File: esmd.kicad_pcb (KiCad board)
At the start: 2 copper layers, 30 x 25 mm, 8 parts, among them J1 Conn_01x04, J2 Conn_01x08, J3 Conn_01x02, J4 Conn_01x02, U2 LM78M05_TO252, U3 74HC245

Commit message: Make it triple.
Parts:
- added C2: 100n, Capacitor_SMD:C_0603_1608Metric, F.Cu at (168.0, 120.0)
- added C3: 100n, Capacitor_SMD:C_0603_1608Metric, F.Cu at (167.9, 134.6)
- added H1: MountingHole, MountingHole:MountingHole_3.2mm_M3, F.Cu at (167.3, 86.1)
- added H2: MountingHole, MountingHole:MountingHole_3.2mm_M3, F.Cu at (167.3, 139.2)
- added J5: Conn_01x04, Connector_JST:JST_XH_B4B-XH-A_1x04_P2.50mm_Vertical, F.Cu at (159.5, 127.2)
- added J6: Conn_01x08, Connector_JST:JST_XH_B6B-XH-A_1x06_P2.50mm_Vertical, F.Cu at (177.4, 139.6)
- added J7: Conn_01x02, Connector_JST:JST_XH_B2B-XH-A_1x02_P2.50mm_Vertical, F.Cu at (158.5, 88.2)
- added R2: 1k, Resistor_SMD:R_0603_1608Metric, F.Cu at (164.6, 120.0)
- added R3: 1k, Resistor_SMD:R_0603_1608Metric, F.Cu at (164.6, 134.6)
- added U1: 74HC245, Package_SO:SSOP-20_5.3x7.2mm_P0.65mm, F.Cu at (167.8, 115.1)
- added U4: 74HC245, Package_SO:SSOP-20_5.3x7.2mm_P0.65mm, F.Cu at (167.8, 129.8)
- J1: footprint Connector_JST:JST_XH_S4B-XH-A_1x04_P2.50mm_Horizontal -> Connector_JST:JST_XH_B4B-XH-A_1x04_P2.50mm_Vertical
- J2: footprint Connector_JST:JST_XH_S6B-XH-A_1x06_P2.50mm_Horizontal -> Connector_JST:JST_XH_B6B-XH-A_1x06_P2.50mm_Vertical
- J3: value Conn_01x02 -> Conn_01x04; footprint Connector_JST:JST_XH_B2B-XH-A_1x02_P2.50mm_Vertical -> Connector_JST:JST_XH_B4B-XH-A_1x04_P2.50mm_Vertical
- J4: value Conn_01x02 -> Conn_01x08; footprint Connector_PinSocket_2.54mm:PinSocket_1x02_P2.54mm_Vertical -> Connector_JST:JST_XH_B6B-XH-A_1x06_P2.50mm_Vertical
- moved J4 37.9 mm to (177.4, 121.0), turned to 90 degrees
- moved J3 26.2 mm to (159.5, 111.7)
- moved C1 3.18 mm to (167.9, 106.2)
- moved R1 3.17 mm to (164.5, 106.2)
- moved U2 3.09 mm to (168.9, 93.2)
- moved U3 3.05 mm to (167.6, 101.1)
- moved J2 0.89 mm to (177.4, 102.3)
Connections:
- net Dir renamed Dir1
- net Dir_out renamed Dir_out1
- net Enable renamed Enable1
- net Enable_out renamed Enable_out1
- net Step renamed Step1
- net Step_out renamed Step_out1
- J3 pad 1: Net-(J3-Pin_1) -> Enable2
- J3 pad 2: GND -> Step2
- J4 pad 1: Net-(J3-Pin_1) -> Dir_out2
- U2 pad 1: Net-(J3-Pin_1) -> Net-(J7-Pin_1)
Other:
- board size 30 x 25 mm -> 25.9 x 60.1 mm
- board text added: "+"
- board text added: "Stepper driver"
- board text added: "https://github.com/bullestock/externalstepperdriver"

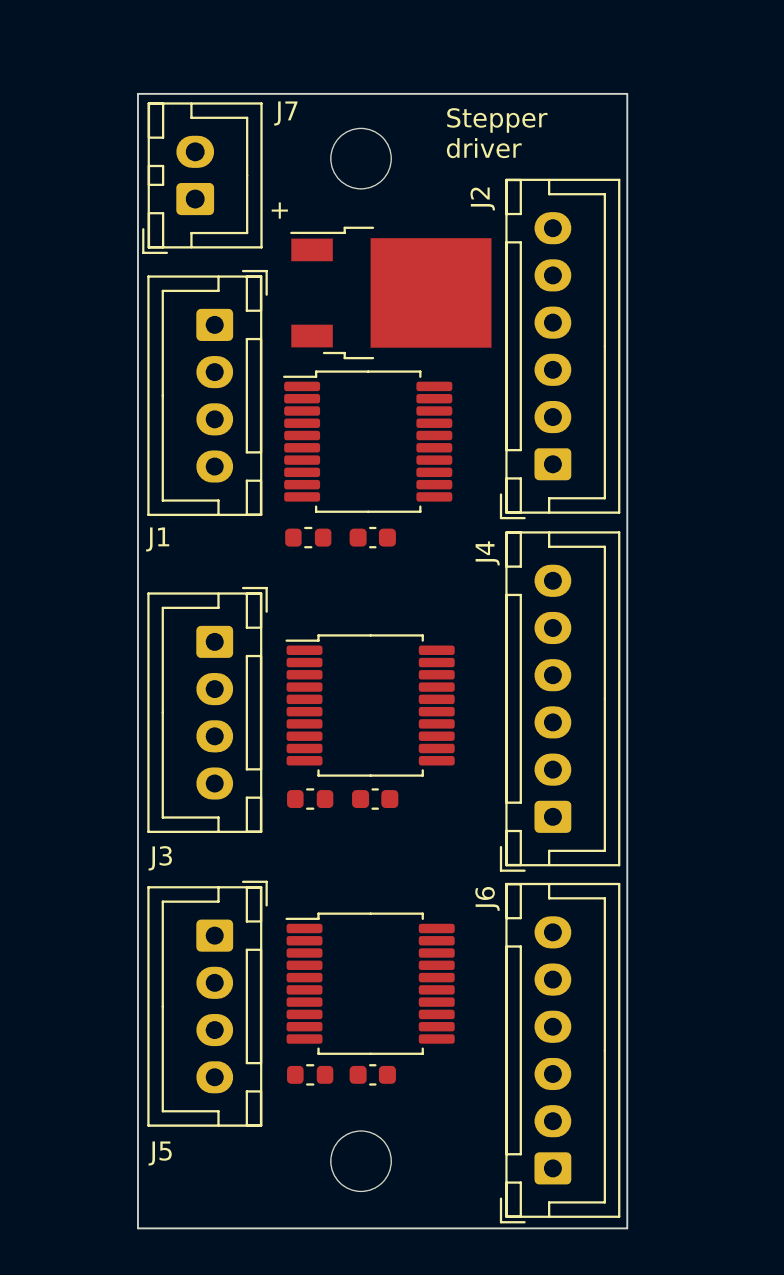
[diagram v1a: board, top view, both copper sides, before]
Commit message: Fix footprints.
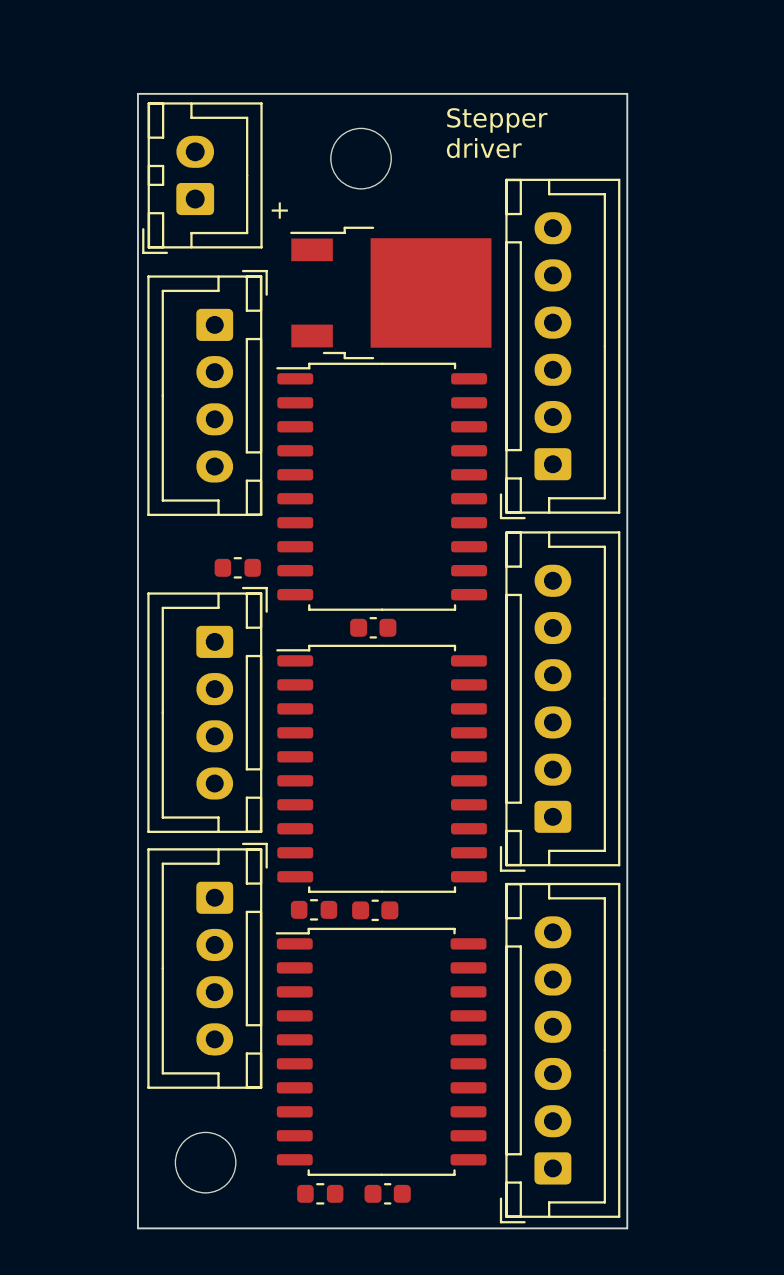
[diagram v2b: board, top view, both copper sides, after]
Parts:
- U1, U3, U4: footprint Package_SO:SSOP-20_5.3x7.2mm_P0.65mm -> Package_SO:SOP-20_7.5x12.8mm_P1.27mm
- moved H2 8.23 mm to (159.0, 139.3)
- moved C3 6.35 mm to (168.7, 140.9)
- moved R3 6.32 mm to (165.1, 140.9), turned to 180 degrees
- moved C2 5.89 mm to (168.0, 125.9)
- moved R2 5.87 mm to (164.8, 125.9), turned to 180 degrees
- moved C1 4.78 mm to (167.9, 110.9)
- moved R1 4.06 mm to (160.7, 107.8), turned to 0 degrees
- moved U4 3.65 mm to (168.3, 133.4)
- moved U1 3.41 mm to (168.4, 118.4)
- moved U3 2.50 mm to (168.4, 103.5)
- moved J5 2.01 mm to (159.5, 125.2)

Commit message: Route.
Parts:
- U1, U3, U4: footprint Package_SO:SOP-20_7.5x12.8mm_P1.27mm -> Package_SO:SO-20_5.3x12.6mm_P1.27mm
- moved R1 5.44 mm to (165.2, 110.9), turned to 180 degrees
- moved C1 0.43 mm to (168.3, 110.9)
- moved R2 0.38 mm to (165.2, 125.9)
- moved C2 0.30 mm to (168.3, 125.9), turned to 180 degrees
- moved U2 0.25 mm to (168.6, 93.2)
- turned C3 to 180 degrees
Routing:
- net GND: track 0.00 -> 199.7 mm, vias 0 -> 4
- net +5V: track 0.00 -> 70.9 mm
- net Net-(U4-A->B): track 0.00 -> 22.7 mm, vias 0 -> 2
- net Net-(U1-A->B): track 0.00 -> 22.3 mm, vias 0 -> 2
- net Net-(U3-A->B): track 0.00 -> 21.7 mm, vias 0 -> 2
- net Enable_out1: track 0.00 -> 12.1 mm
- net Step_out1: track 0.00 -> 9.45 mm
- net Dir1: track 0.00 -> 8.71 mm
- net Enable_out2: track 0.00 -> 8.44 mm
- net Enable3: track 0.00 -> 8.23 mm
- net Step1: track 0.00 -> 7.90 mm
- net Dir3: track 0.00 -> 7.87 mm
- net Enable1: track 0.00 -> 7.86 mm
- net Step3: track 0.00 -> 7.83 mm
- net Dir_out1: track 0.00 -> 7.39 mm
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- added copper zone on B.Cu, net GND
- added copper zone on F.Cu, net GND

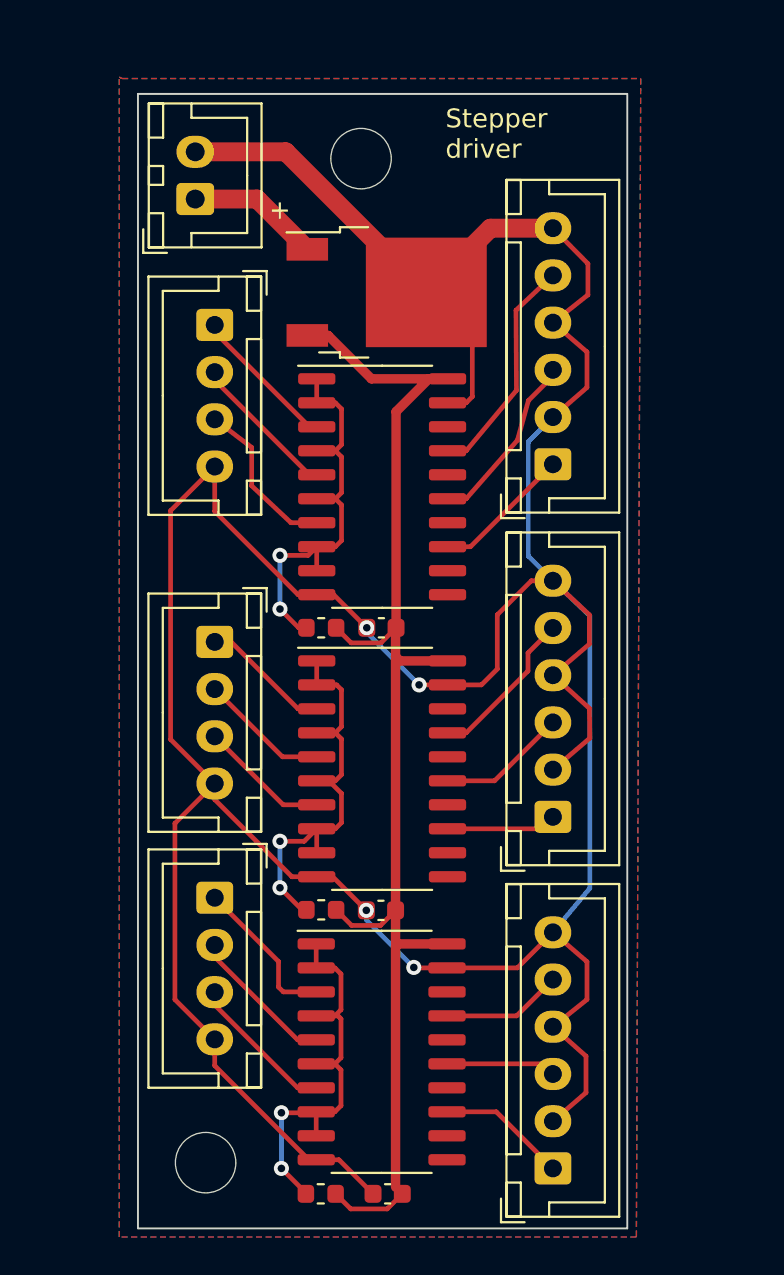
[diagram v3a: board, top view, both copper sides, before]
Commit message: Add support for 5V supply.
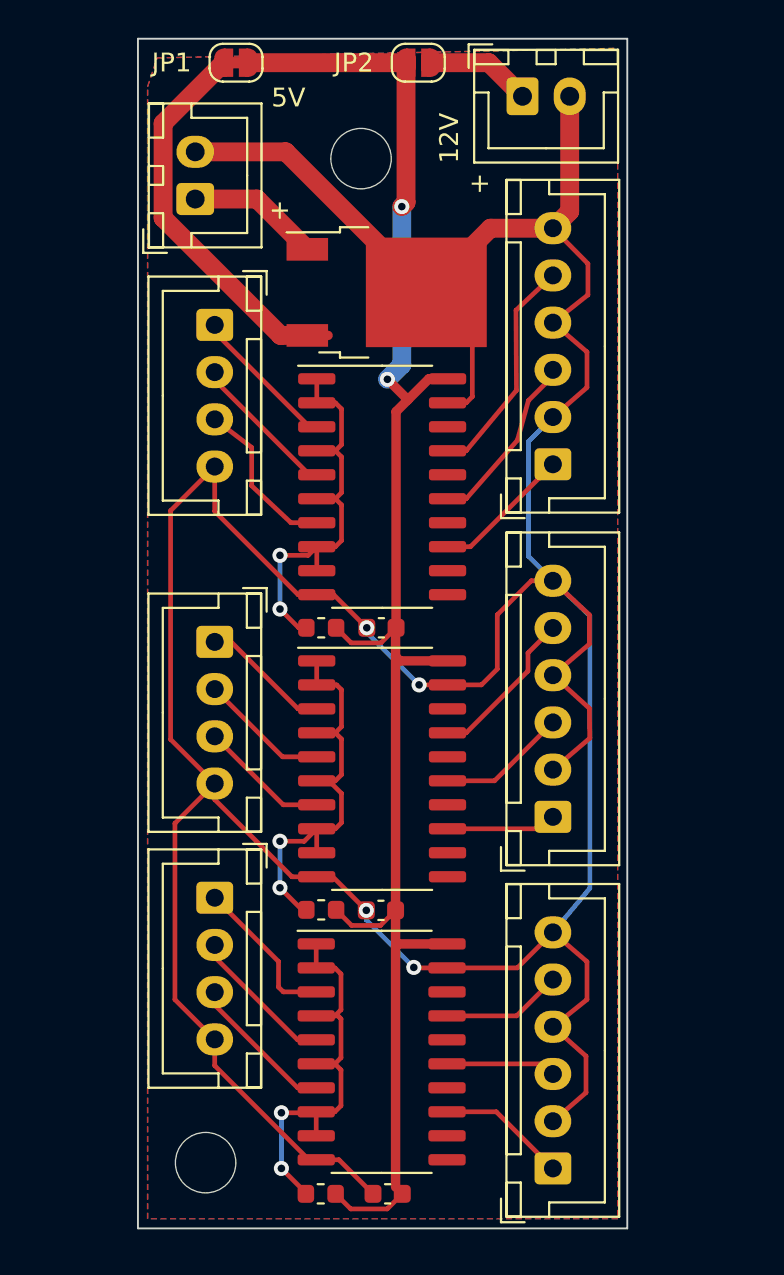
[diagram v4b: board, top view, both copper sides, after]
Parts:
- added J8: Conn_01x02, Connector_JST:JST_XH_B2B-XH-A_1x02_P2.50mm_Vertical, F.Cu at (175.8, 82.8)
- added JP1: Bridge closed, Jumper:SolderJumper-2_P1.3mm_Bridged_RoundedPad1.0x1.5mm, F.Cu at (160.6, 81.0)
- added JP2: Bridge open, Jumper:SolderJumper-2_P1.3mm_Open_RoundedPad1.0x1.5mm, F.Cu at (170.3, 81.0)
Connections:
- U2 pad 3: +5V -> Net-(JP1-B)
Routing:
- net Net-(JP1-B): track 0.00 -> 20.9 mm
- net +5V: track 70.9 -> 89.6 mm, vias 0 -> 2
- net GND: track 199.7 -> 207.1 mm
- net Net-(J8-Pin_1): track 0.00 -> 5.60 mm
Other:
- board size 25.9 x 60.1 mm -> 25.9 x 63 mm
- board text added: "12V"
- board text added: "5V"
- board text removed: "Stepper driver"

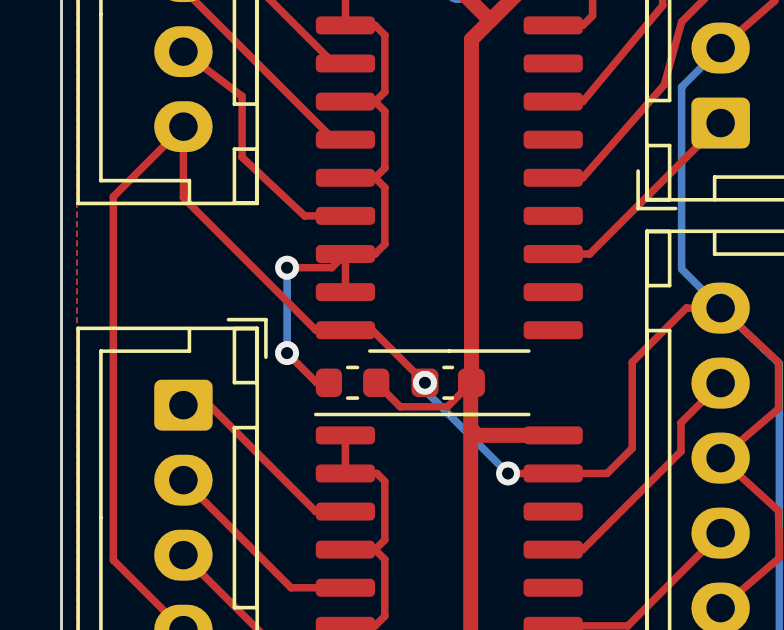
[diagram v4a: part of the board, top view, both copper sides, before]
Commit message: Add power LED.
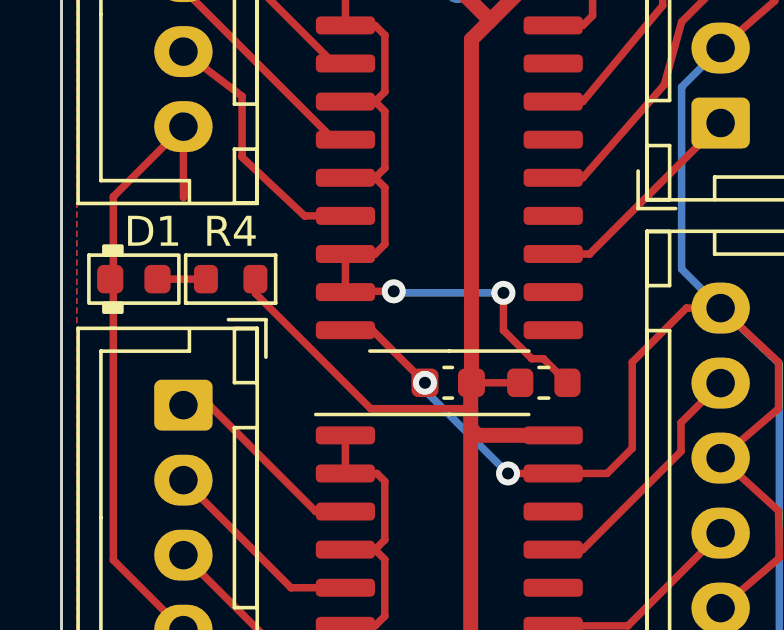
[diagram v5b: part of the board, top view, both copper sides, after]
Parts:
- added D1: LED, PCM_LED_SMD_AKL:LED_0603_1608Metric, F.Cu at (157.9, 107.5)
- added R4: 3k3, PCM_Resistor_SMD_AKL:R_0603_1608Metric, F.Cu at (161.1, 107.5)
- moved R1 6.38 mm to (171.5, 110.9), turned to 0 degrees
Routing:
- net GND: track 207.1 -> 199.8 mm
- net +5V: track 89.6 -> 96.6 mm
- net Net-(U3-A->B): track 21.7 -> 24.3 mm
- net Net-(D1-A): track 0.00 -> 1.61 mm

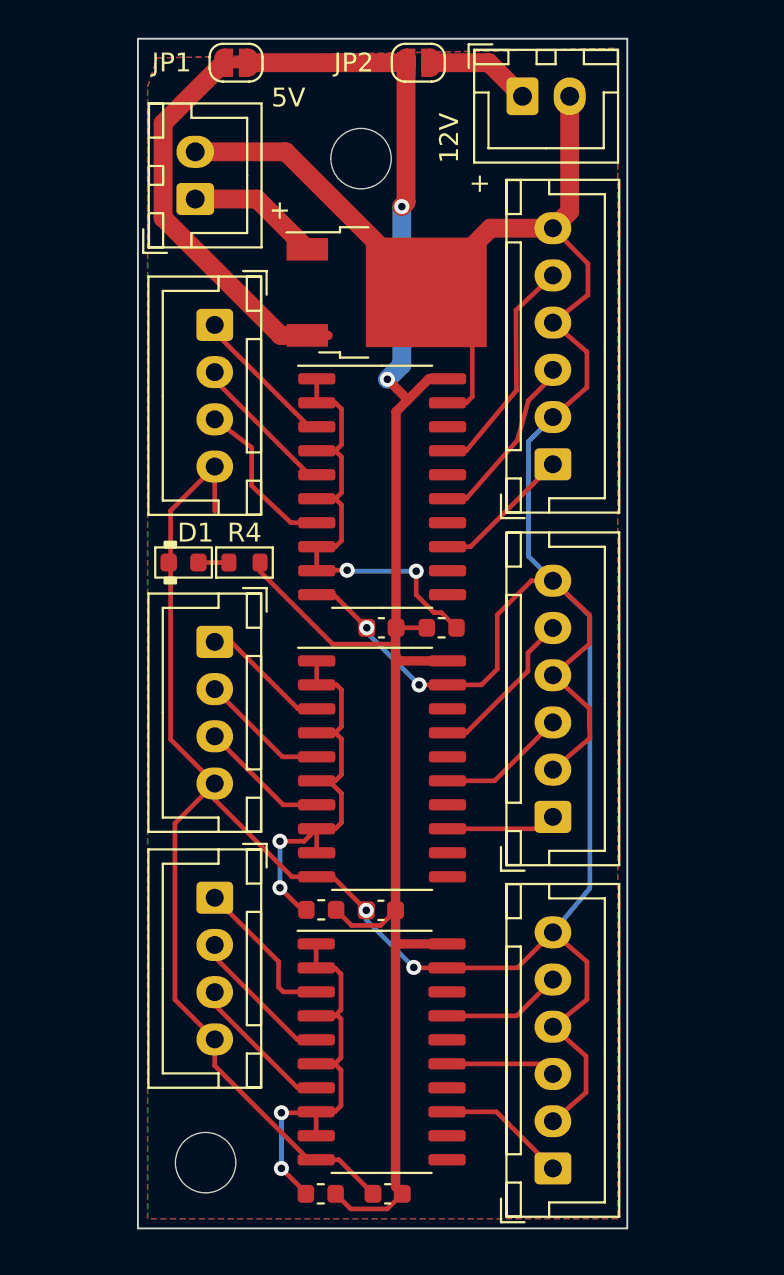
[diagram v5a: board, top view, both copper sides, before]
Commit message: Use only two drivers.
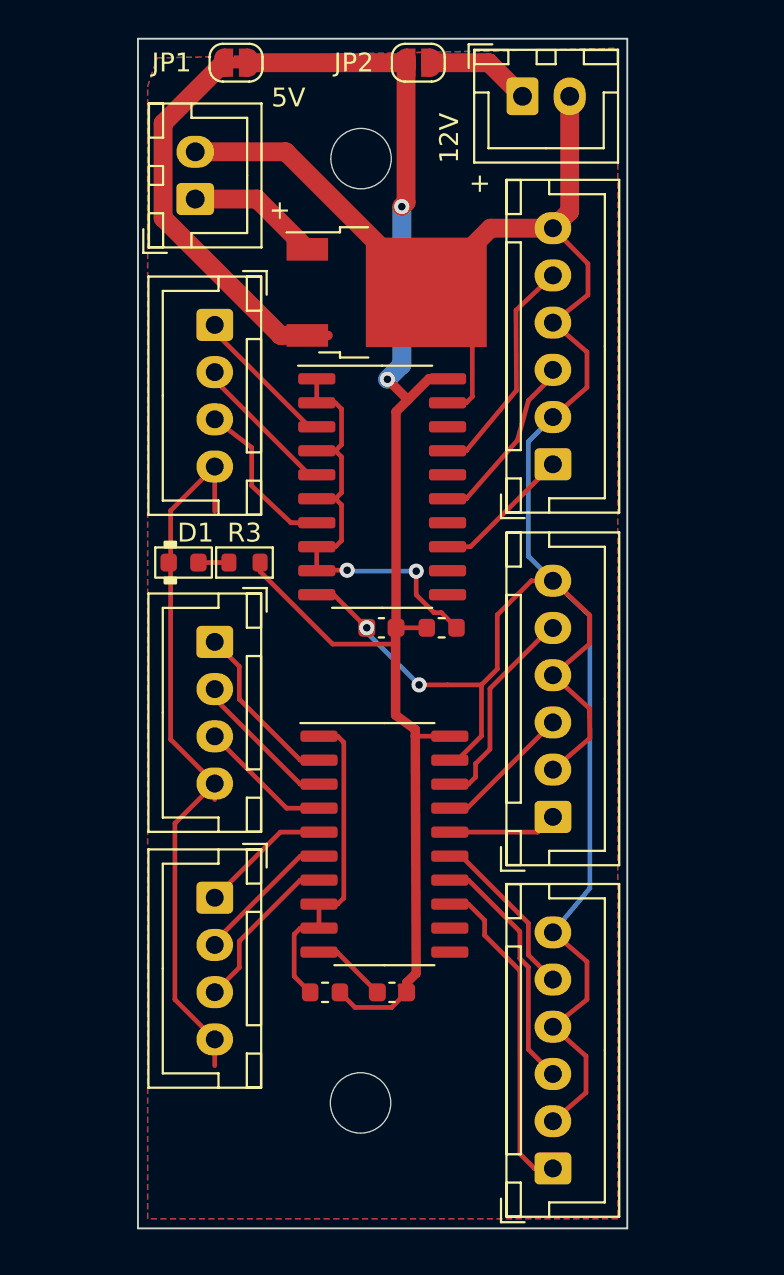
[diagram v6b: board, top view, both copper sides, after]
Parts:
- removed the C2 at (168.3, 125.9)
- removed the R2 at (165.2, 125.9)
- removed the U1 at (168.4, 118.4)
- moved U2 11.0 mm to (168.5, 122.4)
- moved C2 10.7 mm to (168.9, 130.3)
- moved R2 10.7 mm to (165.4, 130.3)
- moved H2 8.79 mm to (167.2, 136.1)
- renumbered C3 to C2, R3 to R2, R4 to R3, U3 to U1, U4 to U2, U2 to U3
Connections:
- R2 pad 2: Net-(U4-A->B) -> Net-(U2-A->B)
- U2 pad 1: Net-(U4-A->B) -> Net-(U2-A->B)
- U2 pad 14: unconnected-(U4-B4-Pad14) -> Step_out3
- U2 pad 15: Step_out3 -> Enable_out3
- U2 pad 16: unconnected-(U4-B2-Pad16) -> Dir_out2
- U2 pad 17: Enable_out3 -> Step_out2
- U2 pad 18: unconnected-(U4-B0-Pad18) -> Enable_out2
- U2 pad 2: Net-(U4-A->B) -> Enable2
- U2 pad 3: Enable3 -> Step2
- U2 pad 4: Net-(U4-A->B) -> Dir2
- U2 pad 5: Step3 -> Enable3
- U2 pad 6: Net-(U4-A->B) -> Step3
- U2 pad 8: Net-(U4-A->B) -> Net-(U2-A->B)
- U2 pad 9: Net-(U4-A->B) -> Net-(U2-A->B)
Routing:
- net GND: track 199.8 -> 174.9 mm, vias 4 -> 2
- net Net-(U4-A->B): track 22.7 -> 0.00 mm, vias 2 -> 0
- net Net-(U1-A->B) (its old number): track 22.3 -> 0.00 mm, vias 2 -> 0
- net Net-(U2-A->B): track 0.00 -> 17.3 mm
- net +5V: track 96.6 -> 79.4 mm
- net Dir_out3: track 6.85 -> 17.4 mm
- net Step_out3: track 5.83 -> 13.1 mm
- net Enable2: track 6.87 -> 10.00 mm
- net Enable_out3: track 6.40 -> 9.16 mm
- net Enable_out2: track 8.44 -> 11.2 mm
- net Dir3: track 7.87 -> 9.48 mm
- net Enable3: track 8.23 -> 6.96 mm
- net Step2: track 6.89 -> 7.90 mm
